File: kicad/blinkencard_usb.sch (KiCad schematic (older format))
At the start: 19 parts, among them J1 USB_B_Micro, U3 CP2102N-A01-GQFN28, U4 MIC5504-1.2YM5, U5 MIC5504-3.3YM5

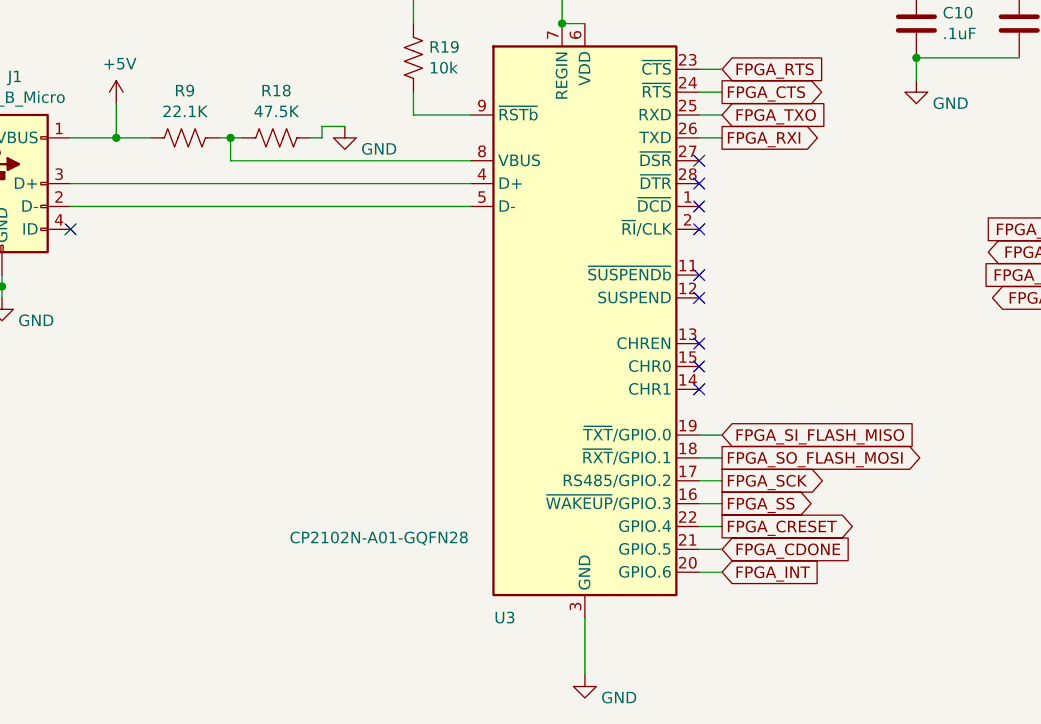
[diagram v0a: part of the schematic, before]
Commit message: Mostly routed
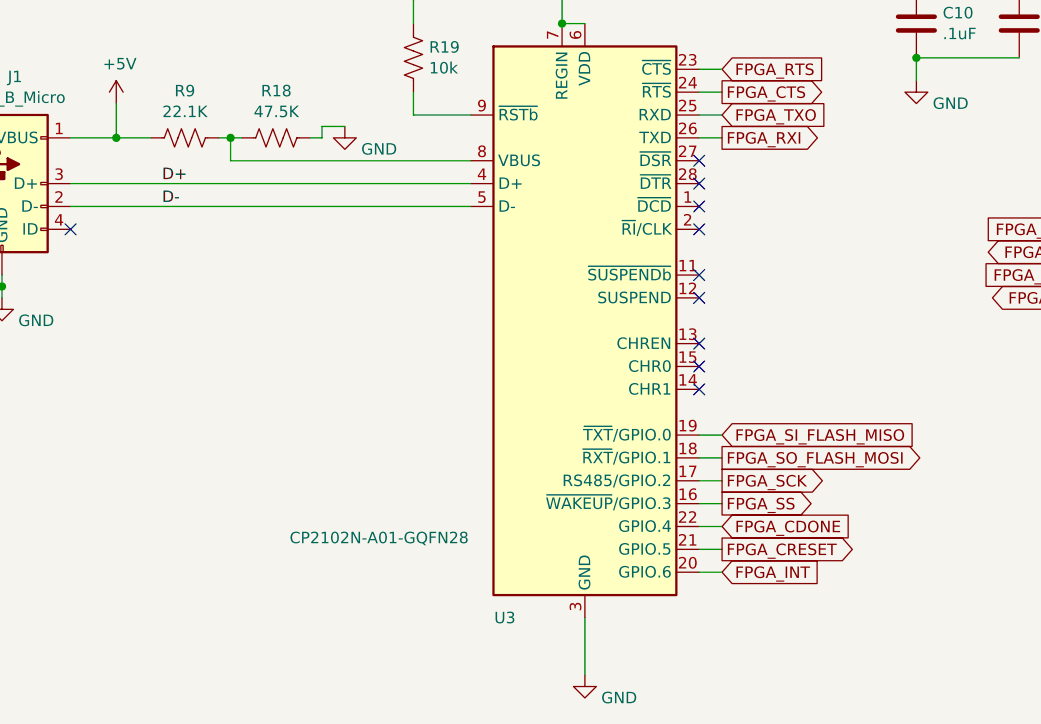
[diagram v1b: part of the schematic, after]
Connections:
- net FPGA_CDONE: now also U3.22 (GPIO.4); no longer U3.21 (GPIO.5)
- net FPGA_CRESET: now also U3.21 (GPIO.5); no longer U3.22 (GPIO.4)
- net D+: now reaches J1.3 (D+), U3.4 (D+)
- net D-: now reaches J1.2 (D-), U3.5 (D-)
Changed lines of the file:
@@
 NoConn ~ 4350 3850
 NoConn ~ 4350 2950
-Text GLabel 4450 4450 2    50   Output ~ 0
+Text GLabel 4450 4550 2    50   Output ~ 0
 FPGA_CRESET
 Text GLabel 4450 4650 2    50   Input ~ 0
@@
 Text GLabel 4450 4350 2    50   Output ~ 0
 FPGA_SS
-Text GLabel 4450 4550 2    50   Input ~ 0
+Text GLabel 4450 4450 2    50   Input ~ 0
 FPGA_CDONE
 Wire Wire Line
@@
 	1    0    0    -1
 $EndComp
+Text Label 2000 2950 0    50   ~ 0
+D+
+Text Label 2000 3050 0    50   ~ 0
+D-
 $EndSCHEMATC

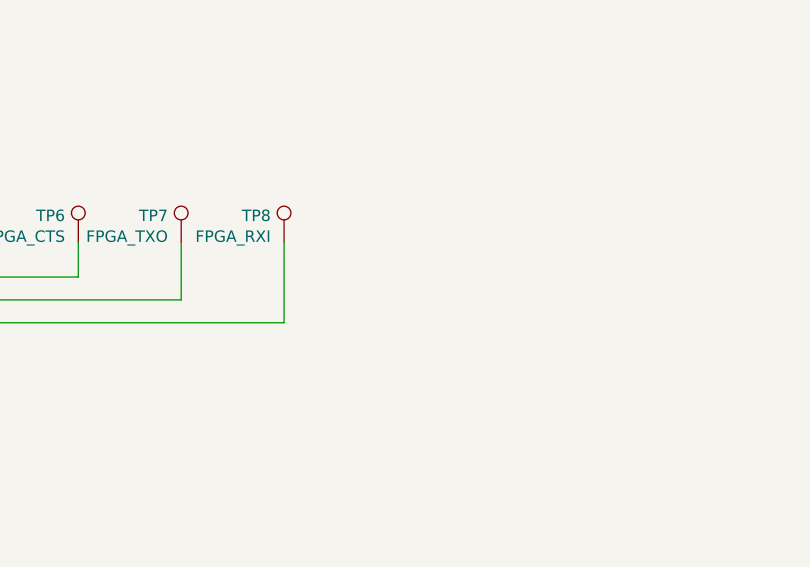
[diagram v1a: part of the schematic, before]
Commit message: Routing complete. DRC passes. Need to fix silk around LEDs and do final check
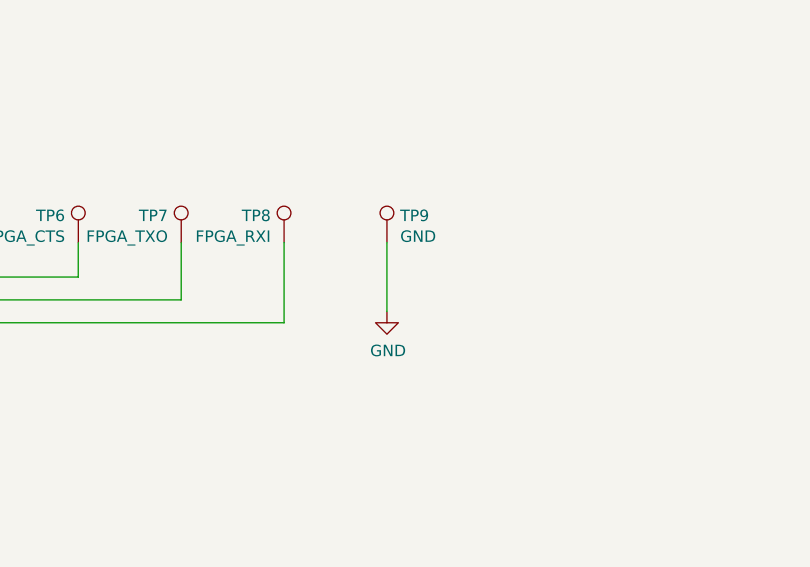
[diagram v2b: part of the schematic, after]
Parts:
- added TP9: GND, TestPoint:TestPoint_Pad_D1.5mm, symbol Connector:TestPoint
- J1: footprint Connector_USB:USB_Micro-B_Molex-105017-0001 -> blinkencard:USB_Micro-B_Molex-105017-0001
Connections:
- net GND: now also TP9.1
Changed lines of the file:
@@
 F 0 "J1" H 1357 3417 50  0000 C CNN
 F 1 "USB_B_Micro" H 1357 3326 50  0000 C CNN
-F 2 "Connector_USB:USB_Micro-B_Molex-105017-0001" H 1450 2900 50  0001 C CNN
+F 2 "blinkencard:USB_Micro-B_Molex-105017-0001" H 1450 2900 50  0001 C CNN
 F 3 "~" H 1450 2900 50  0001 C CNN
 	1    1300 2950
@@
 Text Label 2000 3050 0    50   ~ 0
 D-
+$Comp
+L Connector:TestPoint TP9
+U 1 1 5DDFED95
+P 8250 3100
+F 0 "TP9" H 8308 3218 50  0000 L CNN
+F 1 "GND" H 8308 3127 50  0000 L CNN
+F 2 "TestPoint:TestPoint_Pad_D1.5mm" H 8450 3100 50  0001 C CNN
+F 3 "~" H 8450 3100 50  0001 C CNN
+	1    8250 3100
+	1    0    0    -1
+$EndComp
+$Comp
+L power:GND #PWR0108
+U 1 1 5DDFF59A
+P 8250 3400
+F 0 "#PWR0108" H 8250 3150 50  0001 C CNN
+F 1 "GND" H 8255 3227 50  0000 C CNN
+F 2 "" H 8250 3400 50  0001 C CNN
+F 3 "" H 8250 3400 50  0001 C CNN
+	1    8250 3400
+	1    0    0    -1
+$EndComp
+Wire Wire Line
+	8250 3100 8250 3400
 $EndSCHEMATC

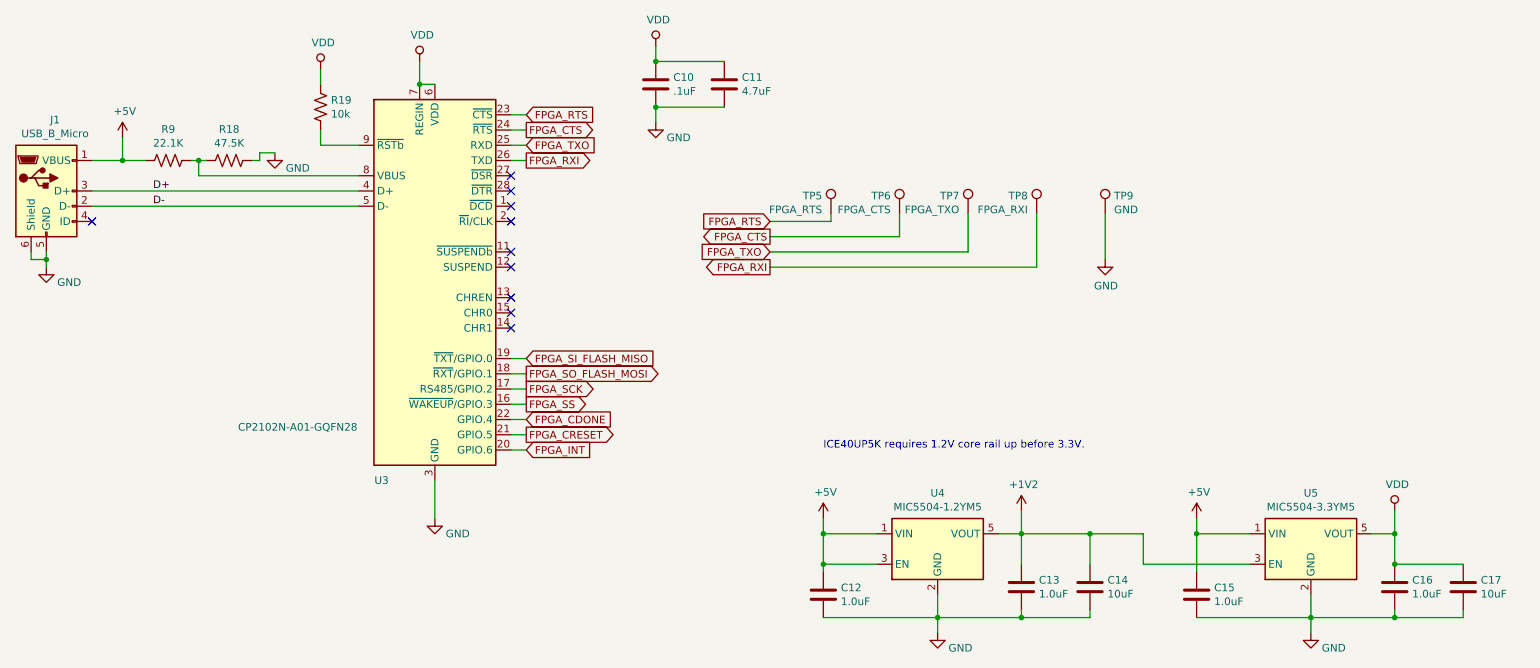
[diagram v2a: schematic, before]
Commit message: Start v1.1 - minor fixes:
- Replace 4.7uF caps with 10uF
- Replace 0.01uF cap in the FPGA VCCPLL filter with 10uF per Lattice's design guideline
- All <1uF caps to 0603 sizes, 1-10uF to 0805
- Make TP? values match between schem and PCB
- Sanitize component values for BOM export consistency
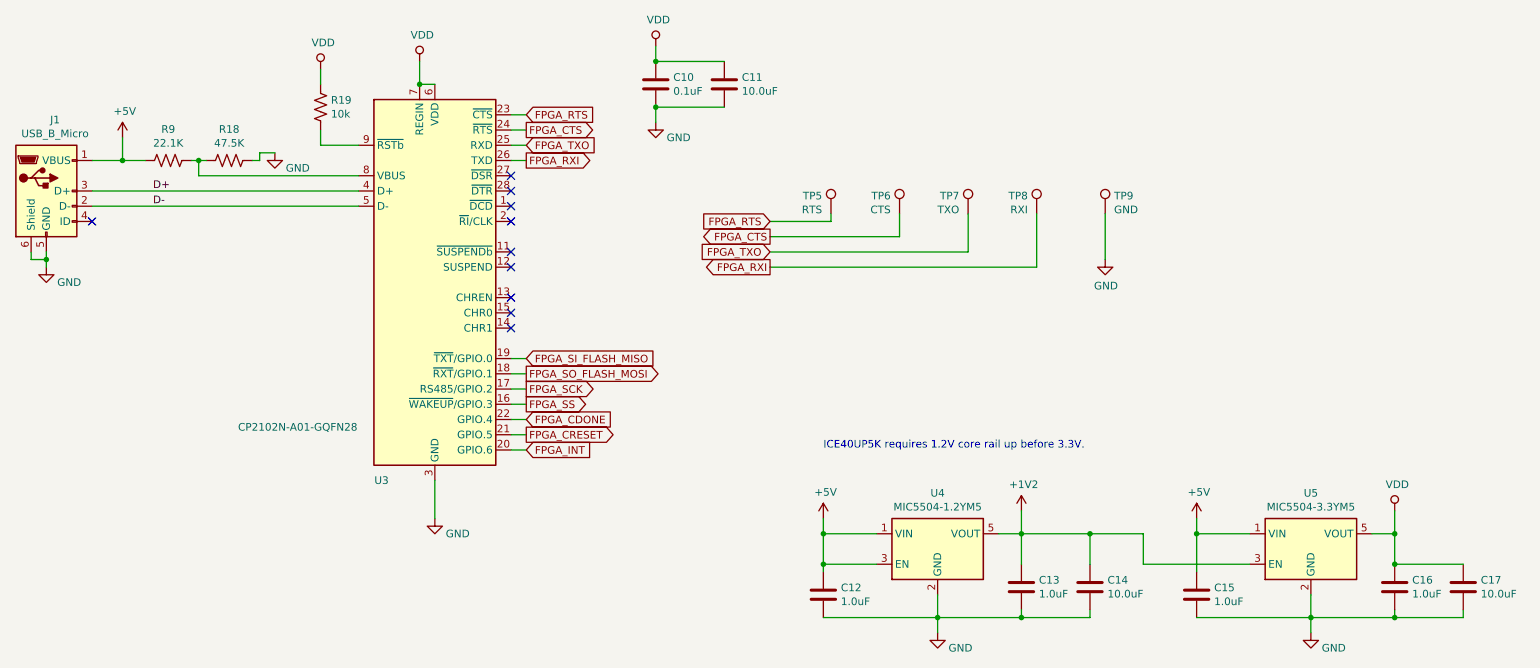
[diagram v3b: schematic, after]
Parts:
- C10: value .1uF -> 0.1uF
- C11: value 4.7uF -> 10.0uF
- C14, C17: value 10uF -> 10.0uF
- TP5: value FPGA_RTS -> RTS
- TP6: value FPGA_CTS -> CTS
- TP7: value FPGA_TXO -> TXO
- TP8: value FPGA_RXI -> RXI
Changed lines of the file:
@@
 P 5300 2250
 F 0 "C10" H 5415 2296 50  0000 L CNN
-F 1 ".1uF" H 5415 2205 50  0000 L CNN
+F 1 "0.1uF" H 5415 2205 50  0000 L CNN
 F 2 "Capacitor_SMD:C_0603_1608Metric" H 5338 2100 50  0001 C CNN
 F 3 "~" H 5300 2250 50  0001 C CNN
@@
 P 5750 2250
 F 0 "C11" H 5865 2296 50  0000 L CNN
-F 1 "4.7uF" H 5865 2205 50  0000 L CNN
+F 1 "10.0uF" H 5865 2205 50  0000 L CNN
 F 2 "Capacitor_SMD:C_0805_2012Metric" H 5788 2100 50  0001 C CNN
 F 3 "~" H 5750 2250 50  0001 C CNN
@@
 FPGA_TXO
 $Comp
-L Connector:TestPoint TP6
-U 1 1 5DEBBAD0
-P 6900 3100
-F 0 "TP6" H 6958 3218 50  0000 L CNN
-F 1 "FPGA_CTS" H 6958 3127 50  0000 L CNN
-F 2 "TestPoint:TestPoint_Pad_D1.5mm" H 7100 3100 50  0001 C CNN
-F 3 "~" H 7100 3100 50  0001 C CNN
-	1    6900 3100
-	-1   0    0    -1
-$EndComp
-$Comp
 L Connector:TestPoint TP7
 U 1 1 5DEBBCBF
 P 7350 3100
 F 0 "TP7" H 7408 3218 50  0000 L CNN
-F 1 "FPGA_TXO" H 7408 3127 50  0000 L CNN
+F 1 "TXO" H 7408 3127 50  0000 L CNN
 F 2 "TestPoint:TestPoint_Pad_D1.5mm" H 7550 3100 50  0001 C CNN
 F 3 "~" H 7550 3100 50  0001 C CNN
@@
 P 7800 3100
 F 0 "TP8" H 7858 3218 50  0000 L CNN
-F 1 "FPGA_RXI" H 7858 3127 50  0000 L CNN
+F 1 "RXI" H 7858 3127 50  0000 L CNN
 F 2 "TestPoint:TestPoint_Pad_D1.5mm" H 8000 3100 50  0001 C CNN
 F 3 "~" H 8000 3100 50  0001 C CNN
@@
 P 6450 3100
 F 0 "TP5" H 6508 3218 50  0000 L CNN
-F 1 "FPGA_RTS" H 6508 3127 50  0000 L CNN
+F 1 "RTS" H 6508 3127 50  0000 L CNN
 F 2 "TestPoint:TestPoint_Pad_D1.5mm" H 6650 3100 50  0001 C CNN
 F 3 "~" H 6650 3100 50  0001 C CNN
@@
 P 8150 5550
 F 0 "C14" H 8265 5596 50  0000 L CNN
-F 1 "10uF" H 8265 5505 50  0000 L CNN
+F 1 "10.0uF" H 8265 5505 50  0000 L CNN
 F 2 "Capacitor_SMD:C_0805_2012Metric" H 8188 5400 50  0001 C CNN
 F 3 "~" H 8150 5550 50  0001 C CNN
@@
 P 10600 5550
 F 0 "C17" H 10715 5596 50  0000 L CNN
-F 1 "10uF" H 10715 5505 50  0000 L CNN
+F 1 "10.0uF" H 10715 5505 50  0000 L CNN
 F 2 "Capacitor_SMD:C_0805_2012Metric" H 10638 5400 50  0001 C CNN
 F 3 "~" H 10600 5550 50  0001 C CNN
@@
 Wire Wire Line
 	8250 3100 8250 3400
+$Comp
+L Connector:TestPoint TP6
+U 1 1 5DEBBAD0
+P 6900 3100
+F 0 "TP6" H 6958 3218 50  0000 L CNN
+F 1 "CTS" H 6958 3127 50  0000 L CNN
+F 2 "TestPoint:TestPoint_Pad_D1.5mm" H 7100 3100 50  0001 C CNN
+F 3 "~" H 7100 3100 50  0001 C CNN
+	1    6900 3100
+	-1   0    0    -1
+$EndComp
 $EndSCHEMATC
